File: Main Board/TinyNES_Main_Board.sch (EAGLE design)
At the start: 109 parts, among them J1 VIDEO, J2 AUDIO, J3 TRRS, J4 USB-C, Q1 PNP, U1 BUFFER, U10 74X1G74, U11 NCS603, U12 74X373, U13 RP2A03, U14 74X139, U15 RP2C02, U16 74X240, U17 BUFFER, U18 APX811, U19 FPF2107, U2 AP2138N, U3 SIT2001B, U4 ICS501, U5 BUFFER, U6 2KB, U7 2KB, U8 PL133-37, U9 74X1G74

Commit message: Main board revisions for production version
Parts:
- removed DA6: DA4-CA-SOT-363, TinyNES_Library:DA4-CA-SOT-363
- removed H2, H3: CTRL, TinyNES_Library:CTRL
- removed R25: 5.1k, TinyNES_Library:RESISTOR-0805
- added H5, H6: CTRL, TinyNES_Library:CTRL
- added P1: 100k, TinyNES_Library:POT
- added RGB: RGB-TOP, TinyNES_Library:RGB-TOP
- added S4: SPDT-EG1213, TinyNES_Library:SPDT-EG1213
- added S5: SPDT-CUS-12TB, TinyNES_Library:SPDT-CUS-12TB
- added U20: FPF2107, TinyNES_Library:FPF2107
- added U21: NOR, TinyNES_Library:NOR
- added U22: XOR, TinyNES_Library:XOR
- C1: value 0.1u -> 1u
- C22: value 330p -> 10u; device TinyNES_Library:CAP-NP-0805 -> TinyNES_Library:CAP-P-1206
- C23: value 10u -> 330p; device TinyNES_Library:CAP-P-1206 -> TinyNES_Library:CAP-NP-0805
- C24: value 330p -> 0.1u
- C25: value 0.1u -> DNP
- C3: value 1u -> 0.1u
- C4: value 0.1u -> 10n
- C6: value 10n -> 0.1u
- DA5: value DA4-CK-SOT-363 -> DA2-S; device TinyNES_Library:DA4-CK-SOT-363 -> TinyNES_Library:DA2-S
- R11: value 68k -> 12k
- R16, R17, R2: value 6.8k -> 10k
- R19: value 6.8k -> 300R
- R20: value 300R -> 270R
- R21: value 270R -> 110R
- R22: value 110R -> 150R
- R23: value 150R -> 5.1k
- S1: value DPDT -> DPDT-LONG; device TinyNES_Library:DPDT -> TinyNES_Library:DPDT-LONG
- S2: value SWITCH -> DPDT; device TinyNES_Library:SWITCH -> TinyNES_Library:DPDT
- S3: value SPDT -> SWITCH; device TinyNES_Library:SPDT -> TinyNES_Library:SWITCH
- U11: value NCS603 -> 74X1G74; device TinyNES_Library:NCS603 -> TinyNES_Library:74X1G74
- U12: value 74X373 -> NCS603; device TinyNES_Library:74X373 -> TinyNES_Library:NCS603
- U13: value RP2A03 -> 74X373; device TinyNES_Library:RP2A03 -> TinyNES_Library:74X373
- U14: value 74X139 -> RP2A03; device TinyNES_Library:74X139 -> TinyNES_Library:RP2A03
- U15: value RP2C02 -> 74X139; device TinyNES_Library:RP2C02 -> TinyNES_Library:74X139
- U16: value 74X240 -> RP2C02; device TinyNES_Library:74X240 -> TinyNES_Library:RP2C02
- U17: value BUFFER -> 74X240; device TinyNES_Library:BUFFER -> TinyNES_Library:74X240
- U18: value APX811 -> BUFFER; device TinyNES_Library:APX811 -> TinyNES_Library:BUFFER
- U19: value FPF2107 -> APX811; device TinyNES_Library:FPF2107 -> TinyNES_Library:APX811
- U2: value AP2138N -> SIT2001B; device TinyNES_Library:AP2138N -> TinyNES_Library:SIT2001B
- U3: value SIT2001B -> ICS501; device TinyNES_Library:SIT2001B -> TinyNES_Library:ICS501
- U4: value ICS501 -> BUFFER; device TinyNES_Library:ICS501 -> TinyNES_Library:BUFFER
- U5: value BUFFER -> 2KB; device TinyNES_Library:BUFFER -> TinyNES_Library:2KB
- U7: value 2KB -> PL133-37; device TinyNES_Library:2KB -> TinyNES_Library:PL133-37
- U8: value PL133-37 -> SIT2001B; device TinyNES_Library:PL133-37 -> TinyNES_Library:SIT2001B
- U9: value 74X1G74 -> AP2138N; device TinyNES_Library:74X1G74 -> TinyNES_Library:AP2138N
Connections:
- new net B: RGB.B, U16.EXT2
- new net G: RGB.G, U16.EXT1
- new net N$14: P1.WIPER, R11.1
- new net N$15: R16.1, U17.1A4, U17.2A4
- new net N$16: S1.3, U8.VDD
- new net N$17: S1.1, U2.VDD
- new net N$18: S1.5, U7.FIN
- new net N$19: S1.4, U2.OUT
- new net N$20: U21.Y, U22.A
- new net N$21: S5.2, U16.A0
- new net N$22: S5.3, U22.Y
- new net R: RGB.R, U16.EXT0
- net !IRQ: now also U14.!IRQ; no longer U13.!IRQ
- net !NMI: now also R17.1, U14.!NMI, U16.!INT; no longer R18.1, U13.!NMI, U15.!INT
- net !OE1: now also C21.2, H5.CUP, U14.!OE1, U17.1!OE; no longer C22.2, H2.CUP, R16.1, U13.!OE1, U16.1!OE
- net !OE2: now also H6.CUP, U14.!OE2, U17.2!OE; no longer H3.CUP, R19.1, U13.!OE2, U16.2!OE
- net !ROMSEL: now also U15.2Y3; no longer U14.2Y3
- net 1Y0-!CS: now also U15.1Y0, U5.!CE; no longer U14.1Y0, U6.!CE
- net 3V3: now also C1.1, C6.1, C8.1, S1.2, U7.VDD, U9.VOUT; no longer C4.1, C5.1, C7.1, U2.VOUT, U3.VDD, U8.VDD
- net A0: now also S5.1, U14.A0, U22.B, U5.A0; no longer U13.A0, U15.A0, U6.A0
- net A1: now also U14.A1, U16.A1, U21.B, U5.A1; no longer U13.A1, U15.A1, U6.A1
- net A10: now also U14.A10, U5.A10; no longer U13.A10, U6.A10
- net A11: now also U14.A11; no longer U13.A11
- net A12: now also U14.A12; no longer U13.A12
- net A13: now also U14.A13, U15.A1; no longer U13.A13, U14.A1
- net A14: now also U14.A14, U15.B1; no longer U13.A14, U14.B1
- net A15: now also U14.A15, U15.B2; no longer U13.A15, U14.B2
- net A2: now also U14.A2, U16.A2, U21.A, U5.A2; no longer U13.A2, U15.A2, U6.A2
- net A3: now also U14.A3, U5.A3; no longer U13.A3, U6.A3
- net A4: now also U14.A4, U5.A4; no longer U13.A4, U6.A4
- net A5: now also U14.A5, U5.A5; no longer U13.A5, U6.A5
- net A6: now also U14.A6, U5.A6; no longer U13.A6, U6.A6
- net A7: now also U14.A7, U5.A7; no longer U13.A7, U6.A7
- net A8: now also U14.A8, U5.A8; no longer U13.A8, U6.A8
- net A9: now also U14.A9, U5.A9; no longer U13.A9, U6.A9
- net ALE: now also U13.C, U16.ALE; no longer U12.C, U15.ALE
- net AUDIO-OUT: now also R22.2; no longer R23.2
- net AUDIO1: now also U14.AUD1; no longer U13.AUD1
- net AUDIO2: now also U14.AUD2; no longer U13.AUD2
- net CIC: now also U4.Y; no longer U5.Y
- net CLK: now also S1.6, U8.OUT; no longer U3.OUT, U8.FIN
- net CLK0: now also U7.CLK0; no longer U8.CLK0
- net CLK1: now also U7.CLK1; no longer U8.CLK1
- net CLK2: now also U7.CLK2; no longer U8.CLK2
- net CLK5X: now also U10.CP, U3.CLK; no longer U4.CLK, U9.CP
- net CLK5X/2: now also U10.Q, U11.CP; no longer U10.CP, U9.Q
- net CLKIN: now also S2.3, U3.X1; no longer S1.3, U4.X1
- net CLKVCC: now also C4.2, C7.1, S2.5, U11.!R!D, U11.!S!D, U11.VCC, U3.OE, U3.S0, U3.VDD; no longer C6.2, C8.1, S1.5, U4.OE, U4.S0, U4.VDD, U9.!R!D, U9.!S!D, U9.VCC
- net CPUCLK: now also S2.1, U11.Q, U14.CLK; no longer S1.1, U10.Q, U13.CLK
- net CPUCLK-SW: now also S2.2; no longer S1.2
- net D0: now also U14.D0, U16.D0, U17.1Y1, U17.2Y1, U5.D0; no longer U13.D0, U15.D0, U16.1Y1, U16.2Y1, U6.D0
- net D1: now also U14.D1, U16.D1, U17.1Y4, U17.2Y4, U5.D1; no longer U13.D1, U15.D1, U6.D1
- net D2: now also U14.D2, U16.D2, U5.D2; no longer U13.D2, U15.D2, U6.D2
- net D3: now also U14.D3, U16.D3, U17.1Y2, U17.2Y2, U5.D3; no longer U13.D3, U15.D3, U16.1Y2, U16.2Y2, U6.D3
- net D4: now also U14.D4, U16.D4, U17.1Y3, U17.2Y3, U5.D4; no longer U13.D4, U15.D4, U16.1Y3, U16.2Y3, U6.D4
- net D5: now also U14.D5, U16.D5, U5.D5; no longer U13.D5, U15.D5, U6.D5
- net D6: now also U14.D6, U16.D6, U5.D6; no longer U13.D6, U15.D6, U6.D6
- net D7: now also U14.D7, U16.D7, U5.D7; no longer U13.D7, U15.D7, U6.D7
- net DQ1: now also U10.!Q, U10.D; no longer U9.!Q, U9.D
- net DQ2: now also U11.!Q, U11.D; no longer U10.!Q, U10.D
- net EXP6-OUT: now also P1.CW, U12B.OUT; no longer R11.1, U11B.OUT
- net G1-2Y1: now also U15.2Y1, U15.G1; no longer U14.2Y1, U14.G1
- net GND: now also C22.C, C23.1, C24.2, C25.1, C4.1, C6.2, DA5.A, H5.GND, H6.GND, R23.1, RGB.GND, S2.4, S3.2, S4.3, U11.GND, U12A.+, U12B.+, U12C.AGND, U12C.PGND, U13.!OC, U14.TST, U15.G2, U16.EXT3, U20.GND, U21.GND, U22.GND, U3.S1, U5.!OE; no longer C22.1, C23.C, C24.1, C25.2, C4.2, C6.1, DA5.1, DA5.2, DA6.COM, H2.GND, H3.GND, R25.1, S1.4, S2.2, S3.3, U11A.+, U11B.+, U11C.AGND, U11C.PGND, U12.!OC, U12.GND, U13.TST, U14.G2, U15.EXT0, U15.EXT1, U15.EXT2, U15.EXT3, U16.1A4, U16.2A4, U4.S1, U6.!OE
- net LEDA: now also R20.1; no longer R21.1
- net LEDK: now also U18.Y; no longer U17.Y
- net M2: now also U14.M2, U15.A2; no longer U13.M2, U14.A2
- net N$1: now also R19.2; no longer R20.2
- net N$10: now also R22.1, U12A.OUT; no longer R23.1, U11A.OUT
- net N$13: now also U12C.CN; no longer U11C.CN
- net N$2: now also R24.2; no longer R25.2
- net N$3: now also R23.2; no longer R24.2
- net N$4: now also U12C.CP; no longer U11C.CP
- net N$5: now also R21.1; no longer R22.1
- net N$6: now also R21.2, RGB.S; no longer R22.2
- net N$7: now also U12B.-; no longer U11B.-
- net N$8: now also U12A.-; no longer U11A.-
- net N$9: now also U12C.VSS; no longer U11C.VSS
- net OUT0: now also DA5.COM, H5.OUT0, H6.OUT0, R18.1, U14.OUT0; no longer C21.2, DA5.3, DA5.4, DA6.3, DA6.4, H2.OUT0, H3.OUT0, R17.1, U13.OUT0
- net P1-D0: now also H5.D0, U17.1A1; no longer H2.D0, U16.1A1
- net P1-D3: now also H5.D3, U17.1A2; no longer H2.D3, U16.1A2
- net P1-D4: now also H5.D4, U17.1A3; no longer H2.D4, U16.1A3
- net P2-D0: now also H6.D0, U17.2A1; no longer H3.D0, U16.2A1
- net P2-D3: now also C23.2, H6.D3, U17.2A2; no longer C24.2, H3.D3, U16.2A2
- net P2-D4: now also H6.D4, U17.2A3; no longer H3.D4, U16.2A3
- net PA0: now also U13.8Q, U6.A0; no longer U12.8Q, U7.A0
- net PA1: now also U13.7Q, U6.A1; no longer U12.7Q, U7.A1
- net PA10: now also U16.PA10; no longer U15.PA10
- net PA11: now also U16.PA11; no longer U15.PA11
- net PA12: now also U16.PA12; no longer U15.PA12
- net PA13: now also U16.PA13; no longer U15.PA13
- net PA2: now also U13.6Q, U6.A2; no longer U12.6Q, U7.A2
- net PA3: now also U13.5Q, U6.A3; no longer U12.5Q, U7.A3
- net PA4: now also U13.4Q, U6.A4; no longer U12.4Q, U7.A4
- net PA5: now also U13.3Q, U6.A5; no longer U12.3Q, U7.A5
- net PA6: now also U13.2Q, U6.A6; no longer U12.2Q, U7.A6
- net PA7: now also U13.1Q, U6.A7; no longer U12.1Q, U7.A7
- net PA8: now also U16.PA8, U6.A8; no longer U15.PA8, U7.A8
- net PA9: now also U16.PA9, U6.A9; no longer U15.PA9, U7.A9
- net PD0: now also U13.8D, U16.PD0, U6.D0; no longer U12.8D, U15.PD0, U7.D0
- net PD1: now also U13.7D, U16.PD1, U6.D1; no longer U12.7D, U15.PD1, U7.D1
- net PD2: now also U13.6D, U16.PD2, U6.D2; no longer U12.6D, U15.PD2, U7.D2
- net PD3: now also U13.5D, U16.PD3, U6.D3; no longer U12.5D, U15.PD3, U7.D3
- net PD4: now also U13.4D, U16.PD4, U6.D4; no longer U12.4D, U15.PD4, U7.D4
- net PD5: now also U13.3D, U16.PD5, U6.D5; no longer U12.3D, U15.PD5, U7.D5
- net PD6: now also U13.2D, U16.PD6, U6.D6; no longer U12.2D, U15.PD6, U7.D6
- net PD7: now also U13.1D, U16.PD7, U6.D7; no longer U12.1D, U15.PD7, U7.D7
- net PPU-!CS: now also U15.1Y1, U16.!CS; no longer U14.1Y1, U15.!CS
- net PPU-!RD: now also C25.2, U16.!RD, U6.!OE; no longer U15.!RD, U7.!OE
- net PPU-!WR: now also U16.!WR, U6.!WE; no longer U15.!WR, U7.!WE
- net PPUCLK: now also U16.CLK; no longer U15.CLK
- net PWR-ON: now also S4.2, U20.ON; no longer S3.2, U19.ON
- net R/!W: now also U14.R/!W, U16.R/!W, U5.!WE; no longer U13.R/!W, U15.R/!W, U6.!WE
- net RESET: now also U14.!RST, U16.!RST, U18.A, U19.!RST, U4.A; no longer U13.!RST, U15.!RST, U17.A, U18.!RST, U5.A
- net RESET-SW: now also S3.1, U19.!MR; no longer S2.1, U18.!MR
- net VCC: now also C22.A, C24.1, C5.1, DA5.K, H5.VCC, H6.VCC, R19.1, R20.2, RGB.VCC, S2.6, U12C.EN, U12C.UVP, U12C.VDD, U19.VCC, U20.VOUT, U21.VCC, U22.VCC, U4.VCC, U9.VIN; no longer C1.1, C23.A, C25.1, DA5.COM, DA6.1, DA6.2, H2.VCC, H3.VCC, R19.2, R20.1, R21.2, S1.6, U11C.EN, U11C.UVP, U11C.VDD, U12.VCC, U19.VOUT, U2.VIN, U7.VCC
- net VIDEO: now also U16.VIDEO; no longer U15.VIDEO
- net VIN: now also S4.1, U20.VIN; no longer S3.1, U19.VIN
- net VRAM-!CS: now also U6.!CE; no longer U7.!CE
- net VRAM-A10: now also U6.A10; no longer U7.A10
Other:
- note added: "21.477272 MHz"
- note added: "26.601712 MHz"
- note added: "TD-TNES-Y-MB"
- note added: "Y"
- note removed: "T"
- note removed: "TD-TNES-T-MB"
- moved on the sheet: C1, C10, C11, C12, C13, C14, C15, C16, C17, C18, C19, C2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

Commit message: Minor cleanup
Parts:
- H1: value CART-72 -> CART
- U14: value RP2A03 -> CPU; device TinyNES_Library:RP2A03 -> TinyNES_Library:CPU
- U16: value RP2C02 -> PPU; device TinyNES_Library:RP2C02 -> TinyNES_Library:PPU
- U20: value FPF2107 -> FPF210X; device TinyNES_Library:FPF2107 -> TinyNES_Library:FPF210X
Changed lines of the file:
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@@
 <setting verticaltext="up"/>
 </settings>
-<grid distance="0.1" unitdist="inch" unit="inch" style="lines" multiple="1" display="no" altdistance="0.025" altunitdist="inch" altunit="inch"/>
+<grid distance="0.1" unitdist="inch" unit="inch" style="lines" multiple="1" display="no" altdistance="0.01" altunitdist="inch" altunit="inch"/>
 <layers>
 <layer number="1" name="Top" color="4" fill="1" visible="no" active="no"/>
@@
 <part name="R17" library="TinyNES_Library" deviceset="RESISTOR" device="-0805" value="10k"/>
 <part name="U1" library="TinyNES_Library" deviceset="BUFFER" device=""/>
-<part name="H1" library="TinyNES_Library" deviceset="CART-72" device="-CONN-VERT" value="CART-72"/>
-<part name="U14" library="TinyNES_Library" deviceset="RP2A03" device=""/>
-<part name="U16" library="TinyNES_Library" deviceset="RP2C02" device=""/>
+<part name="H1" library="TinyNES_Library" deviceset="CART-72" device="-CONN-VERT" value="CART"/>
+<part name="U14" library="TinyNES_Library" deviceset="CPU" device=""/>
+<part name="U16" library="TinyNES_Library" deviceset="PPU" device=""/>
 <part name="C2" library="TinyNES_Library" deviceset="CAP-NP" device="-0805" value="0.1u"/>
 <part name="C3" library="TinyNES_Library" deviceset="CAP-NP" device="-0805" value="0.1u"/>
@@
 <part name="HOLE1" library="TinyNES_Library" deviceset="HOLE" device="-M2.5"/>
 <part name="HOLE7" library="TinyNES_Library" deviceset="HOLE" device="-M2.5"/>
-<part name="U20" library="TinyNES_Library" deviceset="FPF2107" device=""/>
+<part name="U20" library="TinyNES_Library" deviceset="FPF210X" device=""/>
 <part name="R21" library="TinyNES_Library" deviceset="RESISTOR" device="-0805" value="110R"/>
 <part name="C35" library="TinyNES_Library" deviceset="CAP-NP" device="-0805" value="560p"/>

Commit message: main board version updates
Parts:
- H5: value CTRL -> CTRL1
- H6: value CTRL -> CTRL2
- J3: device TinyNES_Library:TRRS -> TinyNES_Library:TRRS-SJ-43514
- Q1: value PNP -> 3906
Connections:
- new net EXT3: RGB.EX3, U16.EXT3
- net AUDIO2-OUT: now also J3.RT; no longer J3.RO
- net GND: no longer U16.EXT3
- net N$12: now also J3.RS; no longer J3.RI
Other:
- note added: "(CLK×5)"
- note added: "(CLK÷2)"
- note added: "(NTSC)"
- note added: "(PAL)"
- note added: "TD-TNES-Z-MB"
- note added: "Z"
- note removed: "TD-TNES-Y-MB"
- note removed: "Y"

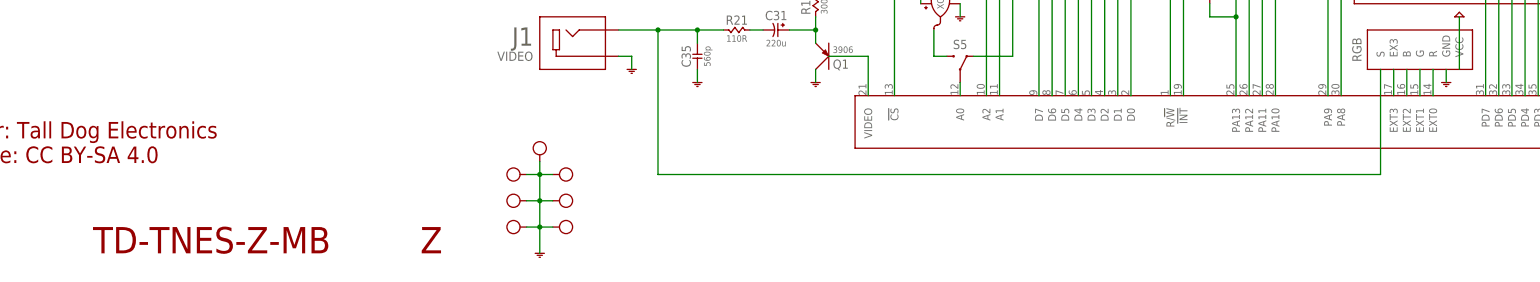
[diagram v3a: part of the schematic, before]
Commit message: Updates in preparation for next production run (Main Board Rev 27)
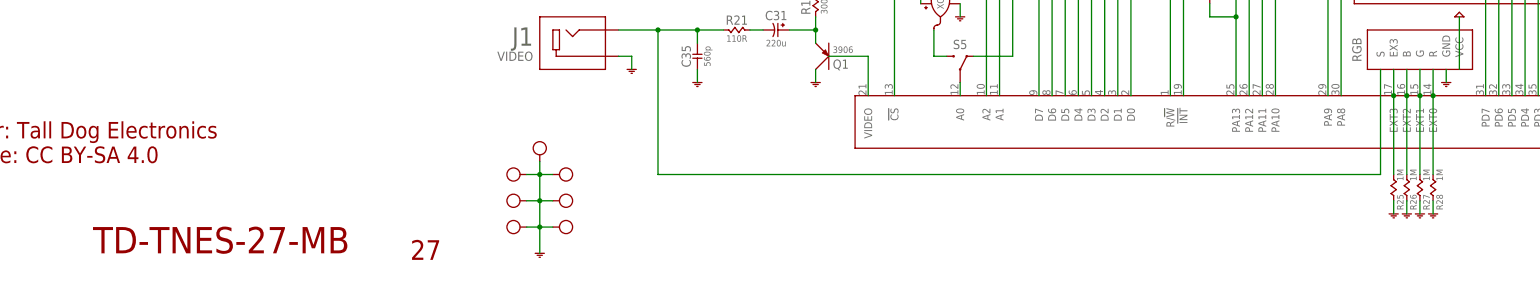
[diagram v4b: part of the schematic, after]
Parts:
- added R25, R26, R27, R28: 1M, TinyNES_Library:RESISTOR-0603
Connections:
- net AUDIO-MIX1 renamed AUDIO-MIX-1
- net AUDIO-OUT renamed AUDIO-MIX-AC
- net AUDIO1 renamed AUDIO1-DC
- net AUDIO1-OUT renamed AUDIO1-AC
- net AUDIO2 renamed AUDIO2-DC
- net AUDIO2-OUT renamed AUDIO2-AC
- net CLK renamed CLK-NTSC
- net EXP6-OUT renamed EXP6-DC
- net N$1 renamed VIDEO1
- net N$10 renamed AUDIO-MIX-DC
- net N$11 renamed EXP6-1
- net N$12 renamed EXP6-AC
- net N$13 renamed CN
- net N$14 renamed EXP6-MIX
- net N$15 renamed D1-PULLUP
- net N$16 renamed VDD-NTSC
- net N$17 renamed VDD-PAL
- net N$18 renamed CLK-FIN
- net N$19 renamed CLK-PAL
- net N$2 renamed CC2
- net N$20 renamed A0-NOR
- net N$21 renamed A0-PPU
- net N$22 renamed A0-XOR
- net N$3 renamed CC1
- net N$4 renamed CP
- net N$5 renamed VIDEO2
- net N$6 renamed VIDEO-OUT
- net N$7 renamed EXP6-2
- net N$8 renamed AUDIO-MIX-2
- net N$9 renamed GND-CAP
- removed net B: RGB.B, U16.EXT2
- removed net G: RGB.G, U16.EXT1
- removed net R: RGB.R, U16.EXT0
- new net RGB-BLUE: R26.2, RGB.B, U16.EXT2
- new net RGB-GREEN: R27.2, RGB.G, U16.EXT1
- new net RGB-RED: R28.2, RGB.R, U16.EXT0
- net EXT3: now also R25.2
- net GND: now also R25.1, R26.1, R27.1, R28.1
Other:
- note added: "27"
- note added: "TD-TNES-27-MB"
- note removed: "TD-TNES-Z-MB"
- note removed: "Z"
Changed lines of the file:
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@@
 <part name="GND38" library="TinyNES_Library" deviceset="GND" device=""/>
 <part name="GND39" library="TinyNES_Library" deviceset="GND" device=""/>
+<part name="R28" library="TinyNES_Library" deviceset="RESISTOR" device="-0603" value="1M"/>
+<part name="R27" library="TinyNES_Library" deviceset="RESISTOR" device="-0603" value="1M"/>
+<part name="R26" library="TinyNES_Library" deviceset="RESISTOR" device="-0603" value="1M"/>
+<part name="R25" library="TinyNES_Library" deviceset="RESISTOR" device="-0603" value="1M"/>
+<part name="GND13" library="TinyNES_Library" deviceset="GND" device=""/>
+<part name="GND40" library="TinyNES_Library" deviceset="GND" device=""/>
+<part name="GND41" library="TinyNES_Library" deviceset="GND" device=""/>
+<part name="GND42" library="TinyNES_Library" deviceset="GND" device=""/>
 </parts>
 <sheets>
 <sheet>
 <plain>
-<text x="98.425" y="10.16" size="5.08" layer="94" align="center">Z</text>
-<text x="33.02" y="10.16" size="5.08" layer="94" align="center-left">TD-TNES-Z-MB</text>
+<text x="100.33" y="6.35" size="3.81" layer="94" ratio="10" align="bottom-right">27</text>
+<text x="33.02" y="10.16" size="5.08" layer="94" align="center-left">TD-TNES-27-MB</text>
 <text x="2.54" y="33.02" size="3.175" layer="94" align="top-left">Author: Tall Dog Electronics
 License: CC BY-SA 4.0</text>
@@
 <instance part="GND38" gate="1" x="200.66" y="53.34" smashed="yes"/>
 <instance part="GND39" gate="1" x="200.66" y="68.58" smashed="yes"/>
+<instance part="R28" gate="G$1" x="292.1" y="20.32" smashed="yes" rot="R90">
+<attribute name="NAME" x="293.37" y="19.05" size="1.27" layer="95" ratio="12" rot="R90" align="center-right"/>
+<attribute name="VALUE" x="293.37" y="21.59" size="1.27" layer="96" rot="R90" align="center-left"/>
+</instance>
+<instance part="R27" gate="G$1" x="289.56" y="20.32" smashed="yes" rot="R90">
+<attribute name="NAME" x="290.83" y="19.05" size="1.27" layer="95" ratio="12" rot="R90" align="center-right"/>
+<attribute name="VALUE" x="290.83" y="21.59" size="1.27" layer="96" rot="R90" align="center-left"/>
+</instance>
+<instance part="R26" gate="G$1" x="287.02" y="20.32" smashed="yes" rot="R90">
+<attribute name="NAME" x="288.29" y="19.05" size="1.27" layer="95" ratio="12" rot="R90" align="center-right"/>
+<attribute name="VALUE" x="288.29" y="21.59" size="1.27" layer="96" rot="R90" align="center-left"/>
+</instance>
+<instance part="R25" gate="G$1" x="284.48" y="20.32" smashed="yes" rot="R90">
+<attribute name="NAME" x="285.75" y="19.05" size="1.27" layer="95" ratio="12" rot="R90" align="center-right"/>
+<attribute name="VALUE" x="285.75" y="21.59" size="1.27" layer="96" rot="R90" align="center-left"/>
+</instance>
+<instance part="GND13" gate="1" x="284.48" y="15.24" smashed="yes"/>
+<instance part="GND40" gate="1" x="287.02" y="15.24" smashed="yes"/>
+<instance part="GND41" gate="1" x="289.56" y="15.24" smashed="yes"/>
+<instance part="GND42" gate="1" x="292.1" y="15.24" smashed="yes"/>
 </instances>
 <busses>
@@
 <pinref part="GND39" gate="1" pin="GND"/>
 </segment>
+<segment>
+<pinref part="R25" gate="G$1" pin="1"/>
+<wire x1="284.48" y1="17.78" x2="284.48" y2="15.24" width="0.1524" layer="91"/>
+<pinref part="GND13" gate="1" pin="GND"/>
+</segment>
+<segment>
+<pinref part="R26" gate="G$1" pin="1"/>
+<wire x1="287.02" y1="17.78" x2="287.02" y2="15.24" width="0.1524" layer="91"/>
+<pinref part="GND40" gate="1" pin="GND"/>
+</segment>
+<segment>
+<pinref part="R27" gate="G$1" pin="1"/>
+<wire x1="289.56" y1="17.78" x2="289.56" y2="15.24" width="0.1524" layer="91"/>
+<pinref part="GND41" gate="1" pin="GND"/>
+</segment>
+<segment>
+<pinref part="R28" gate="G$1" pin="1"/>
+<wire x1="292.1" y1="17.78" x2="292.1" y2="15.24" width="0.1524" layer="91"/>
+<pinref part="GND42" gate="1" pin="GND"/>
+</segment>
 </net>
 <net name="PA13" class="0">
@@
 </segment>
 </net>
-<net name="AUDIO2" class="0">
+<net name="AUDIO2-DC" class="0">
 <segment>
 <wire x1="66.04" y1="134.62" x2="60.96" y2="134.62" width="0.1524" layer="91"/>
@@
 </segment>
 </net>
-<net name="AUDIO1" class="0">
+<net name="AUDIO1-DC" class="0">
 <segment>
 <pinref part="R9" gate="G$1" pin="2"/>
@@
 </segment>
 </net>
-<net name="AUDIO-MIX1" class="0">
+<net name="AUDIO-MIX-1" class="0">
 <segment>
 <wire x1="99.06" y1="170.18" x2="96.52" y2="170.18" width="0.1524" layer="91"/>
@@
 </segment>
 </net>
-<net name="AUDIO-OUT" class="0">
+<net name="AUDIO-MIX-AC" class="0">
 <segment>
 <pinref part="R22" gate="G$1" pin="2"/>
@@
 </segment>
 </net>
-<net name="CLK" class="0">
+<net name="CLK-NTSC" class="0">
 <segment>
 <pinref part="U8" gate="G$1" pin="OUT"/>
@@
 </segment>
 </net>
-<net name="AUDIO1-OUT" class="0">
+<net name="AUDIO1-AC" class="0">
 <segment>
 <pinref part="C29" gate="G$1" pin="2"/>
@@
 </segment>
 </net>
-<net name="AUDIO2-OUT" class="0">
+<net name="AUDIO2-AC" class="0">
 <segment>
 <pinref part="C28" gate="G$1" pin="2"/>
@@
 </segment>
 </net>
-<net name="EXP6-OUT" class="0">
+<net name="EXP6-DC" class="0">
 <segment>
 <pinref part="U12" gate="B" pin="OUT"/>
@@
 </segment>
 </net>
-<net name="N$2" class="0">
+<net name="CC2" class="0">
 <segment>
 <pinref part="J4" gate="G$1" pin="CC2"/>
@@
 </segment>
 </net>
-<net name="N$3" class="0">
+<net name="CC1" class="0">
 <segment>
 <pinref part="J4" gate="G$1" pin="CC1"/>
@@
 </segment>
 </net>
-<net name="N$1" class="0">
+<net name="VIDEO1" class="0">
 <segment>
 <pinref part="Q1" gate="G$1" pin="E"/>
@@
 </segment>
 </net>
-<net name="N$5" class="0">
+<net name="VIDEO2" class="0">
 <segment>
 <pinref part="C31" gate="G$1" pin="C"/>
@@
 </segment>
 </net>
-<net name="N$6" class="0">
+<net name="VIDEO-OUT" class="0">
 <segment>
 <pinref part="R21" gate="G$1" pin="2"/>
@@
 </segment>
 </net>
-<net name="N$8" class="0">
+<net name="AUDIO-MIX-2" class="0">
 <segment>
 <wire x1="81.28" y1="177.8" x2="88.9" y2="177.8" width="0.1524" layer="91"/>
@@
 </segment>
 </net>
-<net name="N$13" class="0">
+<net name="CN" class="0">
 <segment>
 <pinref part="C11" gate="G$1" pin="1"/>
@@
 </segment>
 </net>
-<net name="N$10" class="0">
+<net name="AUDIO-MIX-DC" class="0">
 <segment>
 <pinref part="R14" gate="G$1" pin="2"/>
@@
 </segment>
 </net>
-<net name="N$4" class="0">
+<net name="CP" class="0">
 <segment>
 <pinref part="U12" gate="C" pin="CP"/>
@@
 </segment>
 </net>
-<net name="N$9" class="0">
+<net name="GND-CAP" class="0">
 <segment>
 <pinref part="C12" gate="G$1" pin="2"/>
@@
 </segment>
 </net>
-<net name="N$11" class="0">
+<net name="EXP6-1" class="0">
 <segment>
 <pinref part="R13" gate="G$1" pin="1"/>
@@
 </segment>
 </net>
-<net name="N$7" class="0">
+<net name="EXP6-2" class="0">
 <segment>
 <pinref part="U12" gate="B" pin="-"/>
@@
 </segment>
 </net>
-<net name="N$12" class="0">
+<net name="EXP6-AC" class="0">
 <segment>
 <pinref part="J3" gate="G$1" pin="RS"/>
@@
 </segment>
 </net>
-<net name="N$15" class="0">
+<net name="D1-PULLUP" class="0">
 <segment>
 <pinref part="U17" gate="G$1" pin="2A4"/>
@@
 </segment>
 </net>
-<net name="B" class="0">
+<net name="RGB-BLUE" class="0">
 <segment>
 <pinref part="U16" gate="G$1" pin="EXT2"/>
 <wire x1="287.02" y1="38.1" x2="287.02" y2="43.18" width="0.1524" layer="91"/>
 <pinref part="RGB" gate="G$1" pin="B"/>
-</segment>
-</net>
-<net name="G" class="0">
+<pinref part="R26" gate="G$1" pin="2"/>
+<wire x1="287.02" y1="38.1" x2="287.02" y2="22.86" width="0.1524" layer="91"/>
+<junction x="287.02" y="38.1"/>
+</segment>
+</net>
+<net name="RGB-GREEN" class="0">
 <segment>
 <pinref part="U16" gate="G$1" pin="EXT1"/>
 <wire x1="289.56" y1="38.1" x2="289.56" y2="43.18" width="0.1524" layer="91"/>
 <pinref part="RGB" gate="G$1" pin="G"/>
-</segment>
-</net>
-<net name="R" class="0">
+<pinref part="R27" gate="G$1" pin="2"/>
+<wire x1="289.56" y1="38.1" x2="289.56" y2="22.86" width="0.1524" layer="91"/>
+<junction x="289.56" y="38.1"/>
+</segment>
+</net>
+<net name="RGB-RED" class="0">
 <segment>
 <pinref part="U16" gate="G$1" pin="EXT0"/>
 <wire x1="292.1" y1="38.1" x2="292.1" y2="43.18" width="0.1524" layer="91"/>
 <pinref part="RGB" gate="G$1" pin="R"/>
-</segment>
-</net>
-<net name="N$14" class="0">
+<pinref part="R28" gate="G$1" pin="2"/>
+<wire x1="292.1" y1="38.1" x2="292.1" y2="22.86" width="0.1524" layer="91"/>
+<junction x="292.1" y="38.1"/>
+</segment>
+</net>
+<net name="EXP6-MIX" class="0">
 <segment>
 <pinref part="R11" gate="G$1" pin="1"/>
@@
 </segment>
 </net>
-<net name="N$16" class="0">
+<net name="VDD-NTSC" class="0">
 <segment>
 <pinref part="S1" gate="G$1" pin="3"/>
@@
 </segment>
 </net>
-<net name="N$17" class="0">
+<net name="VDD-PAL" class="0">
 <segment>
 <pinref part="S1" gate="G$1" pin="1"/>
@@
 </segment>
 </net>
-<net name="N$18" class="0">
+<net name="CLK-FIN" class="0">
 <segment>
 <pinref part="S1" gate="G$1" pin="5"/>
@@
 </segment>
 </net>
-<net name="N$19" class="0">
+<net name="CLK-PAL" class="0">
 <segment>
 <pinref part="S1" gate="G$1" pin="4"/>
@@
 </segment>
 </net>
-<net name="N$20" class="0">
+<net name="A0-NOR" class="0">
 <segment>
 <wire x1="195.58" y1="66.04" x2="195.58" y2="60.96" width="0.1524" layer="91"/>
@@
 </segment>
 </net>
-<net name="N$21" class="0">
+<net name="A0-PPU" class="0">
 <segment>
 <pinref part="S5" gate="G$1" pin="2"/>
@@
 </segment>
 </net>
-<net name="N$22" class="0">
+<net name="A0-XOR" class="0">
 <segment>
 <pinref part="S5" gate="G$1" pin="3"/>
@@
 <pinref part="RGB" gate="G$1" pin="EX3"/>
 <wire x1="284.48" y1="38.1" x2="284.48" y2="43.18" width="0.1524" layer="91"/>
-</segment>
-</net>
+<pinref part="R25" gate="G$1" pin="2"/>
+<wire x1="284.48" y1="38.1" x2="284.48" y2="22.86" width="0.1524" layer="91"/>
+<junction x="284.48" y="38.1"/>
+</segment>
+</net>
